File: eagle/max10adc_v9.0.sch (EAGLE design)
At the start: 206 parts, among them IC1 MAX19506, IC2 MAX19506, J1 MOLEX_BNC_73100-0105, J2 MOLEX_BNC_73100-0105, J3 MOLEX_BNC_73100-0105, J4 MOLEX_BNC_73100-0105, K1 AQY21SOP, K2 AQY21SOP, K3 AQY21SOP, K4 AQY21SOP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

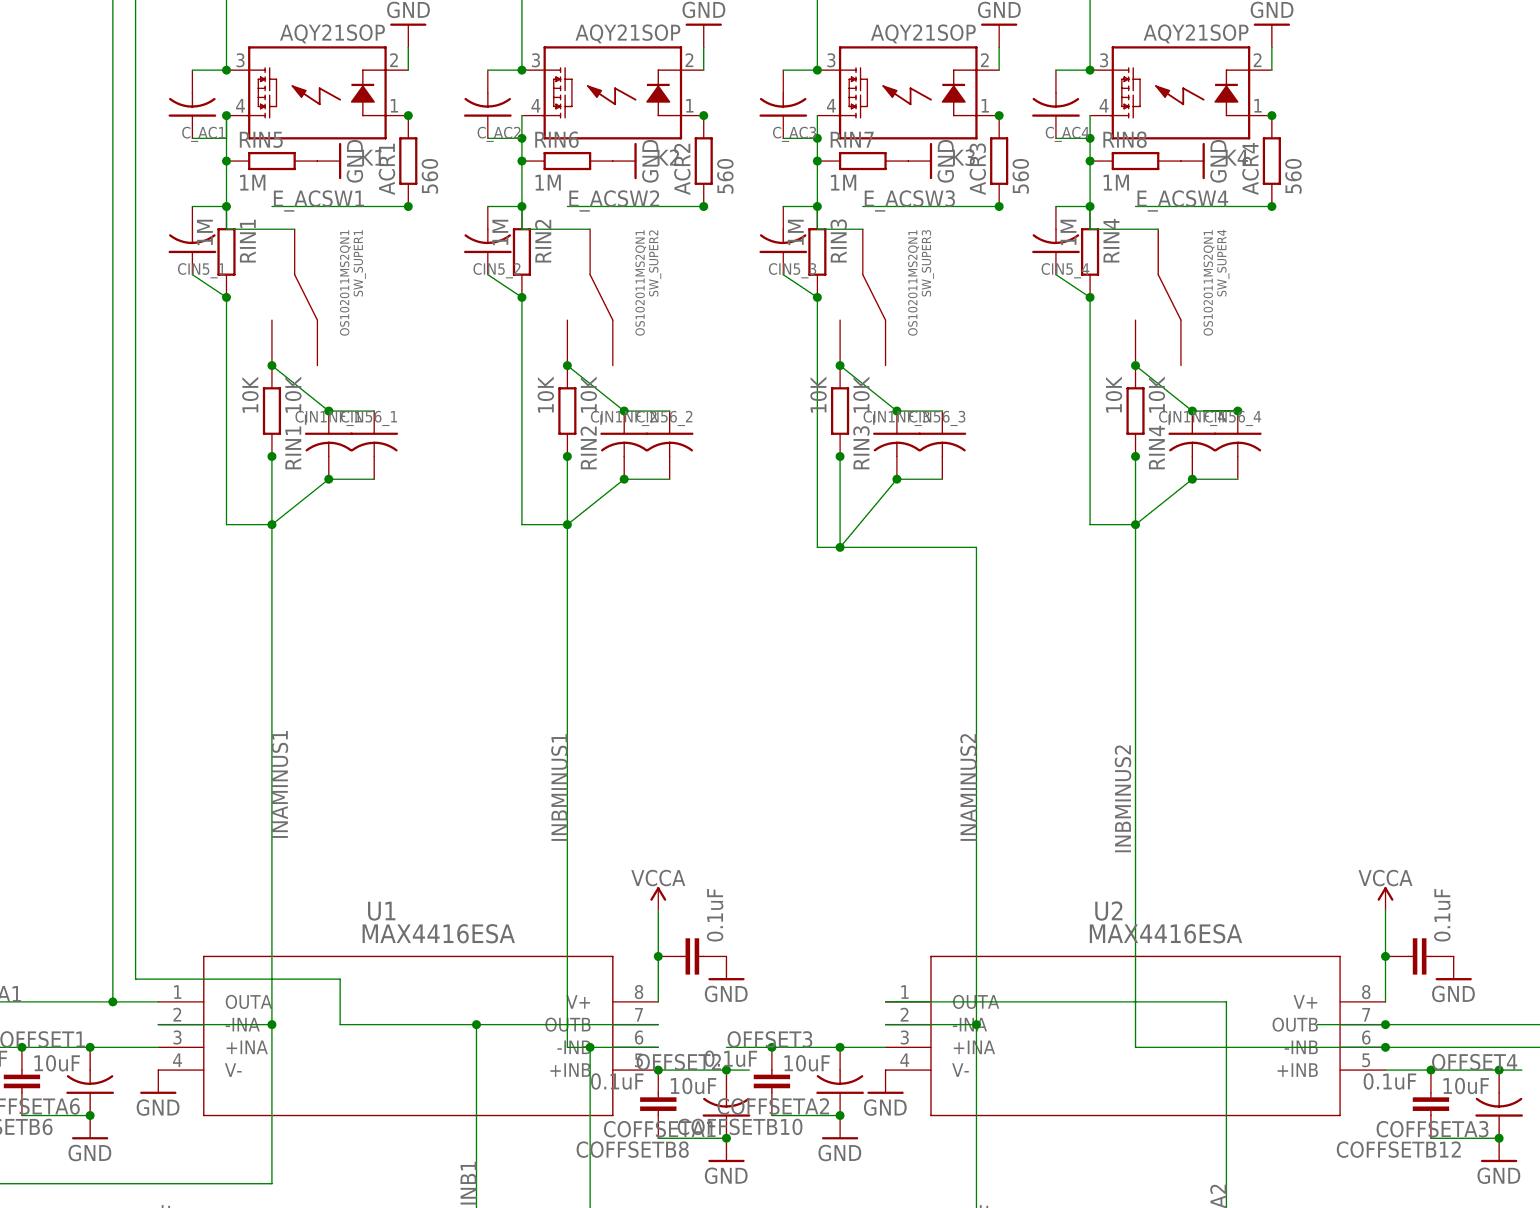
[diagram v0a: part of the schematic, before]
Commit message: v9, with 10M, 1.1M, and 11k input resistors, and rerouted
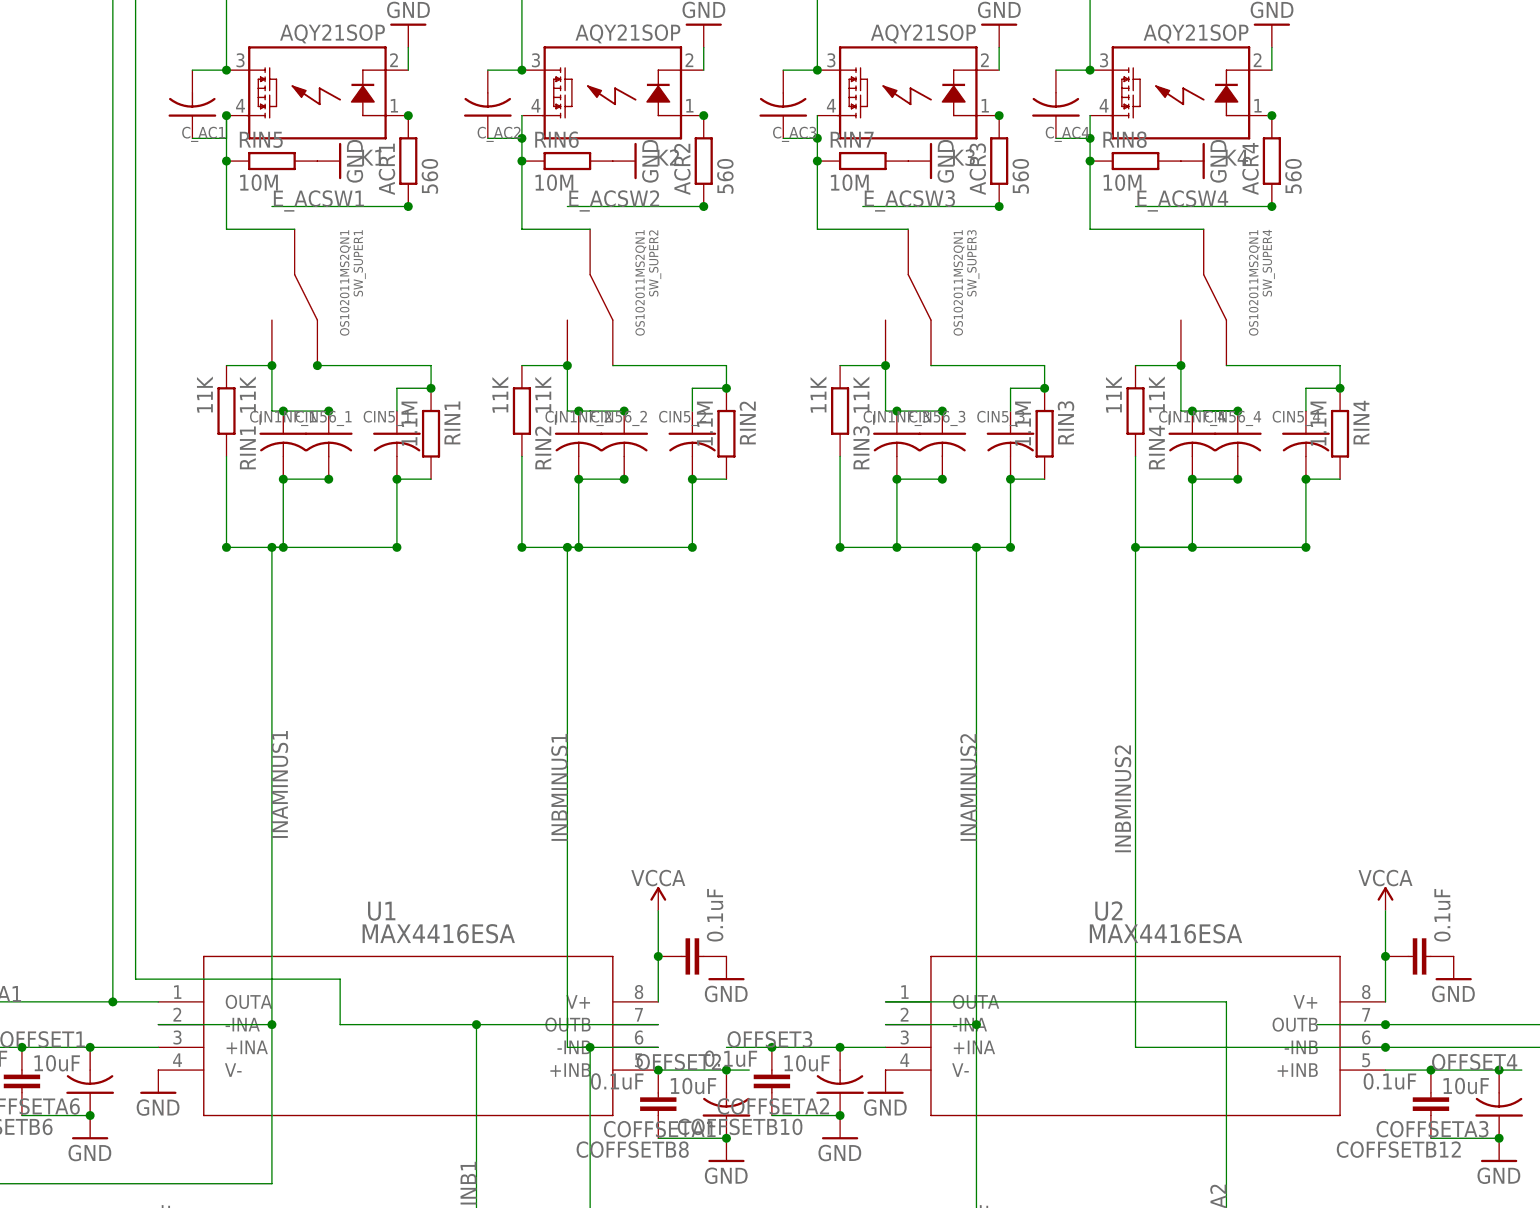
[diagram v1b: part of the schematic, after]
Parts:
- removed RIN1_10K, RIN2_10K: 10K, resistor:R-EU_R0805
- added RIN1_11K, RIN2_11K: 11K, resistor:R-EU_R0805
- RIN1, RIN2, RIN3, RIN4: value 1M -> 1.1M; MPN MF-RES-0805-1M -> CRCW08051M10FKEA
- RIN3_11K, RIN4_11K: value 10K -> 11K; MPN MF-RES-0805-10K -> CRCW080511K0FKEA
- RIN5, RIN6, RIN7, RIN8: value 1M -> 10M; MPN MF-RES-0805-1M -> CRCW080510M0FKEB
- renumbered RIN3_10K to RIN3_11K, RIN4_10K to RIN4_11K
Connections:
- removed net N$41: CIN5_4.2, C_AC4.1, K4.DS1, RIN4.1, RIN8.1, SW_SUPER4.C
- new net N$37: CIN5_1.1, RIN1.1, SW_SUPER1.1
- new net N$42: CIN5_3.1, RIN3.1, SW_SUPER3.1
- new net N$50: C_AC4.1, K4.DS1, RIN8.1, SW_SUPER4.C
- new net N$52: CIN5_4.1, RIN4.1, SW_SUPER4.1
- new net N$61: CIN5_2.1, RIN2.1, SW_SUPER2.1
- net INAMINUS1: now also CIN5_1.2, RIN1_11K.2; no longer CIN5_1.1, RIN1_10K.2
- net INAMINUS2: now also CIN5_3.2; no longer CIN5_3.1
- net INBMINUS1: now also CIN5_2.2, RIN2_11K.2; no longer CIN5_2.1, RIN2_10K.2
- net INBMINUS2: now also CIN5_4.2; no longer CIN5_4.1
- net N$10: no longer CIN5_1.2, RIN1.1
- net N$15: no longer CIN5_2.2, RIN2.1
- net N$20: now also RIN1_11K.1; no longer RIN1_10K.1
- net N$38: now also RIN2_11K.1; no longer RIN2_10K.1
- net N$39: no longer CIN5_3.2, RIN3.1
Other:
- moved on the sheet: CIN1NF_1, CIN1NF_2, CIN56_1, CIN56_2, CIN5_1, CIN5_2, CIN5_3, CIN5_4, RIN1, RIN2, RIN3, RIN4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

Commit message: cleanup schematic
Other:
- note added: "ADCs"
- note added: "FPGA"
- note added: "Front end gain and offset"
- note added: "Front end oversampling switches"
- note added: "Front ends"
- note added: "IO expanders"
- note added: "JTAG interface"
- note added: "LEDs"
- note added: "Left side pinouts"
- note added: "Offset DAC"
- note added: "Oscillator"
- note added: "Power regulation and decoupling"
- note added: "Right side pinouts"
- note added: "Serial to USB interface"
- note added: "Top pinouts"
- moved on the sheet: ACR1, ACR2, ACR3, ACR4, C-AIN1, C-AIN2, C-AIN3, C-AIN4, C0DD1_A, C0DD2_A, C0DD2_B, CADD1_A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
